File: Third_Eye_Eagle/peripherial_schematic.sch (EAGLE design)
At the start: 1 part

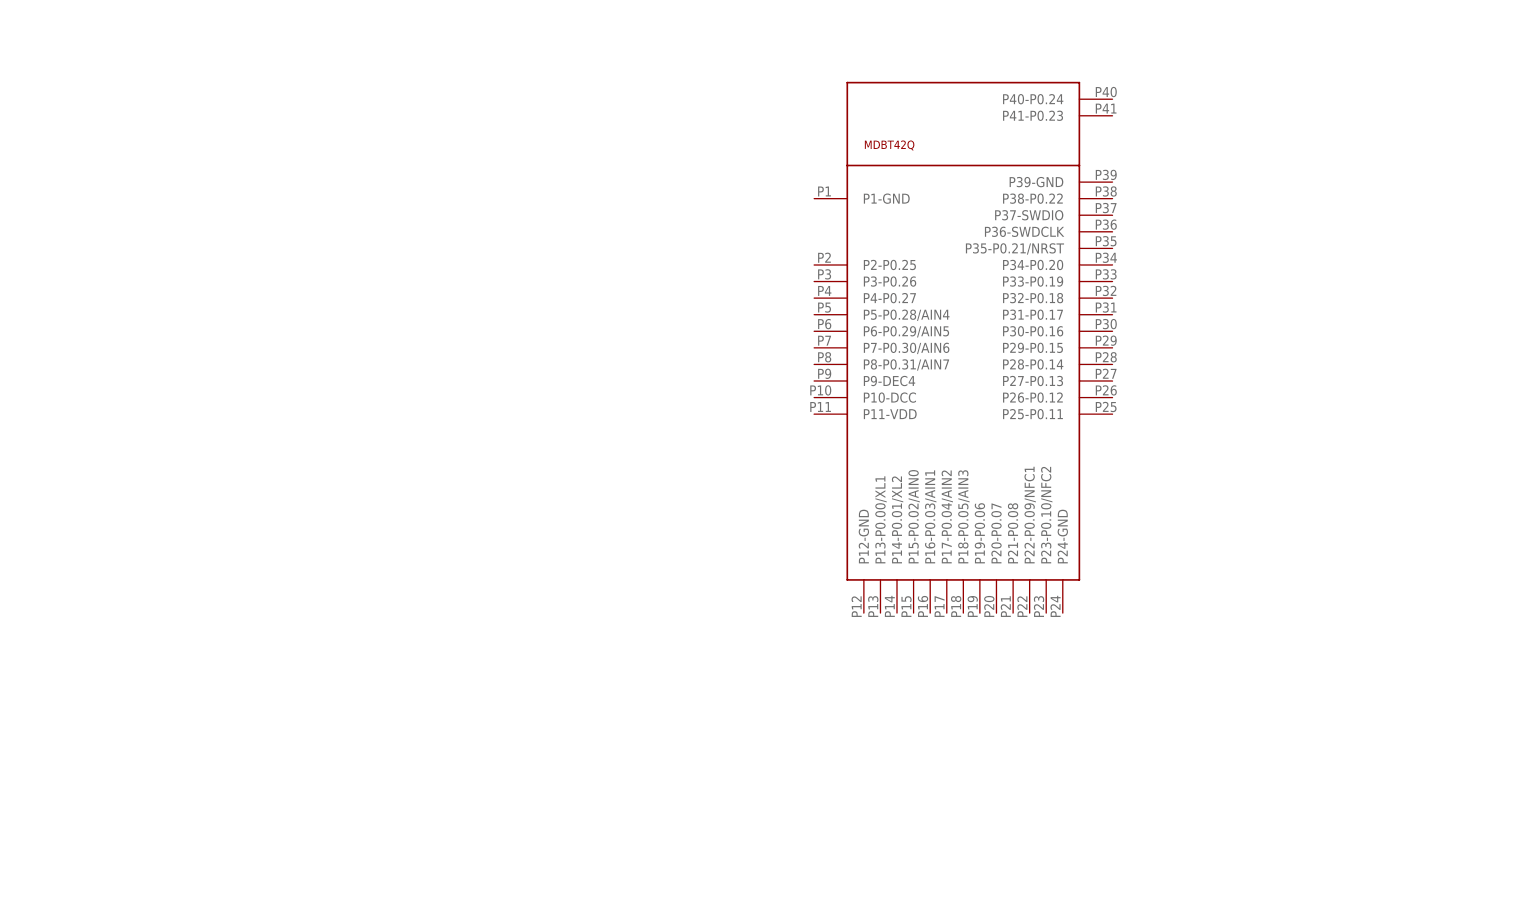
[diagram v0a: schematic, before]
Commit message: Updated Eagle LIbrary and git ignore the eagle temp files
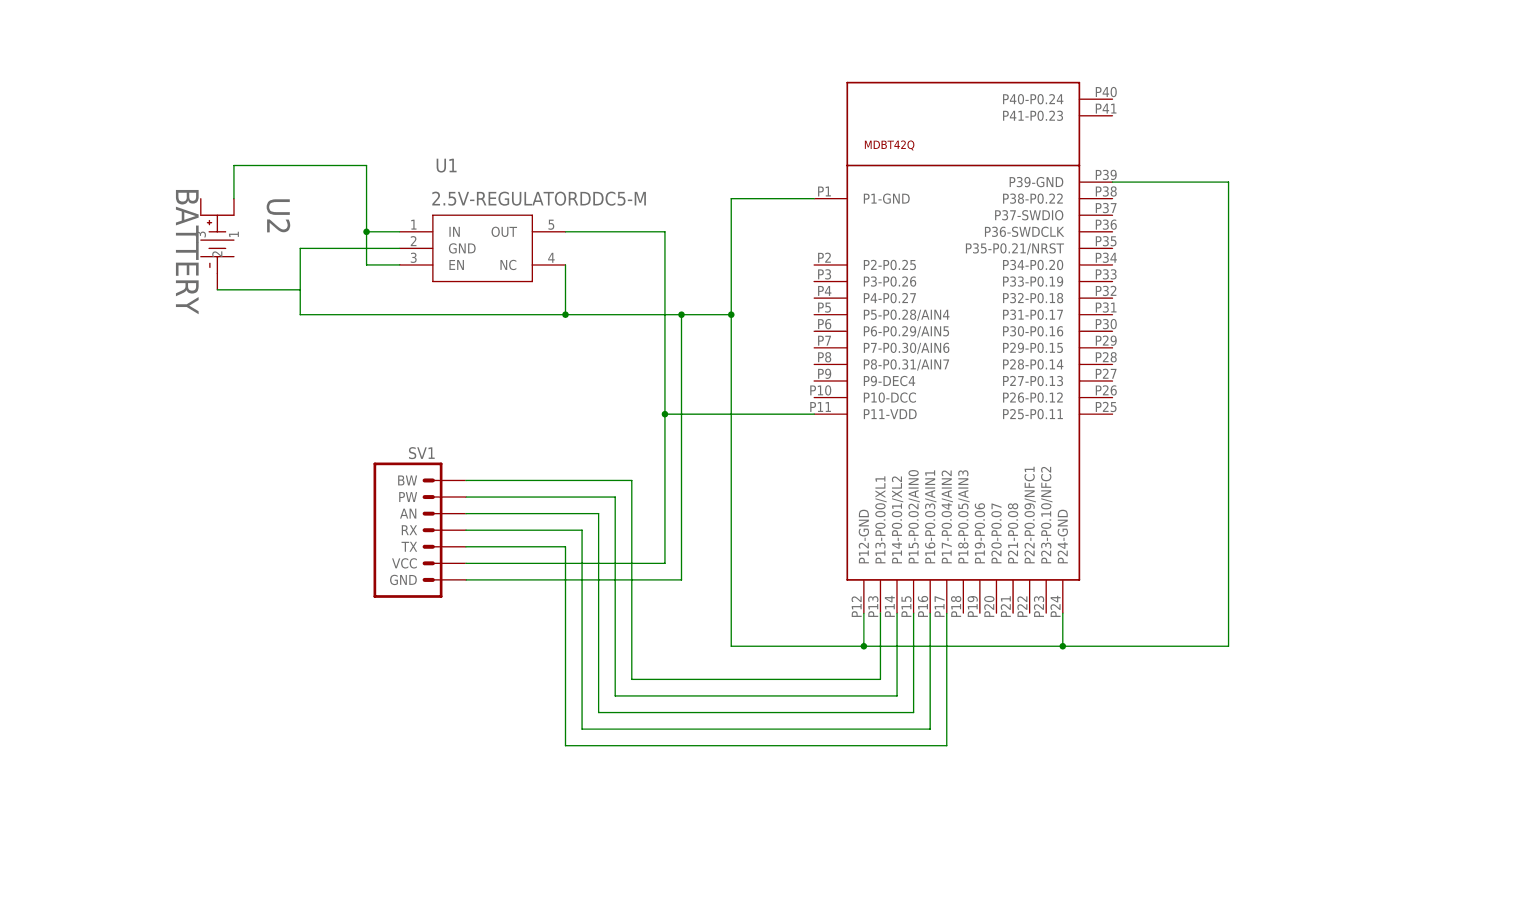
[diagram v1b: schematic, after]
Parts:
- added SV1: (no value), third_eye:SENSORHEADER
- added U1: 2.5V-REGULATORDDC5-M, third_eye:2.5V-REGULATORDDC5-M
- added U2: BATTERY, third_eye:BATTERY
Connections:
- new net N$1: U1.EN, U1.IN, U2.1
- new net N$2: SV1.GND, U$1.P1-GND, U$1.P12-GND, U$1.P24-GND, U$1.P39-GND, U1.GND, U1.NC, U2.2
- new net N$3: SV1.AN, U$1.P15-P0.02/AIN0
- new net N$4: SV1.VCC, U$1.P11-VDD, U1.OUT
- new net N$5: SV1.PW, U$1.P14-P0.01/XL2
- new net N$7: SV1.RX, U$1.P16-P0.03/AIN1
- new net N$8: SV1.TX, U$1.P17-P0.04/AIN2
- new net N$9: SV1.BW, U$1.P13-P0.00/XL1
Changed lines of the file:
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@@
 <setting verticaltext="up"/>
 </settings>
-<grid distance="0.1" unitdist="inch" unit="inch" style="lines" multiple="1" display="no" altdistance="0.01" altunitdist="inch" altunit="inch"/>
+<grid distance="0.1" unitdist="inch" unit="inch" style="dots" multiple="1" display="yes" altdistance="0.01" altunitdist="inch" altunit="inch"/>
 <layers>
 <layer number="1" name="Top" color="4" fill="1" visible="no" active="no"/>
@@
 <parts>
 <part name="U$1" library="third_eye" deviceset="MDBT42Q" device=""/>
+<part name="SV1" library="third_eye" deviceset="SENSORHEADER" device="" package3d_urn="urn:adsk.eagle:package:8341/1"/>
+<part name="U2" library="third_eye" deviceset="BATTERY" device=""/>
+<part name="U1" library="third_eye" deviceset="2.5V-REGULATOR" device="DDC5-M"/>
 </parts>
 <sheets>
@@
 <instances>
 <instance part="U$1" gate="G$1" x="58.42" y="53.34" smashed="yes"/>
+<instance part="SV1" gate="1" x="-38.1" y="20.32" smashed="yes">
+<attribute name="VALUE" x="-39.37" y="7.62" size="1.778" layer="96"/>
+<attribute name="NAME" x="-39.37" y="31.242" size="1.778" layer="95"/>
+</instance>
+<instance part="U2" gate="BAT" x="-66.04" y="71.12" smashed="yes" rot="R270">
+<attribute name="NAME" x="-60.96" y="71.3994" size="3.4798" layer="95" ratio="10" rot="SR270"/>
+<attribute name="VALUE" x="-74.93" y="72.8726" size="3.4798" layer="96" ratio="10" rot="SR270"/>
+</instance>
+<instance part="U1" gate="A" x="-43.18" y="66.04" smashed="yes">
+<attribute name="NAME" x="-35.2044" y="75.1586" size="2.0828" layer="95" ratio="6" rot="SR0"/>
+<attribute name="VALUE" x="-35.8394" y="70.0786" size="2.0828" layer="96" ratio="6" rot="SR0"/>
+</instance>
 </instances>
 <busses>
 </busses>
 <nets>
+<net name="N$1" class="0">
+<segment>
+<pinref part="U1" gate="A" pin="IN"/>
+<wire x1="-40.64" y1="66.04" x2="-45.72" y2="66.04" width="0.1524" layer="91"/>
+<wire x1="-45.72" y1="66.04" x2="-45.72" y2="76.2" width="0.1524" layer="91"/>
+<wire x1="-45.72" y1="76.2" x2="-66.04" y2="76.2" width="0.1524" layer="91"/>
+<pinref part="U2" gate="BAT" pin="1"/>
+<wire x1="-66.04" y1="76.2" x2="-66.04" y2="71.12" width="0.1524" layer="91"/>
+<pinref part="U1" gate="A" pin="EN"/>
+<wire x1="-40.64" y1="60.96" x2="-45.72" y2="60.96" width="0.1524" layer="91"/>
+<wire x1="-45.72" y1="60.96" x2="-45.72" y2="66.04" width="0.1524" layer="91"/>
+<junction x="-45.72" y="66.04"/>
+</segment>
+</net>
+<net name="N$2" class="0">
+<segment>
+<pinref part="U2" gate="BAT" pin="2"/>
+<wire x1="-68.58" y1="57.15" x2="-55.88" y2="57.15" width="0.1524" layer="91"/>
+<pinref part="U1" gate="A" pin="GND"/>
+<wire x1="-55.88" y1="57.15" x2="-55.88" y2="63.5" width="0.1524" layer="91"/>
+<wire x1="-55.88" y1="63.5" x2="-40.64" y2="63.5" width="0.1524" layer="91"/>
+<pinref part="U1" gate="A" pin="NC"/>
+<wire x1="-15.24" y1="60.96" x2="-15.24" y2="53.34" width="0.1524" layer="91"/>
+<wire x1="-15.24" y1="53.34" x2="-55.88" y2="53.34" width="0.1524" layer="91"/>
+<wire x1="-55.88" y1="53.34" x2="-55.88" y2="57.15" width="0.1524" layer="91"/>
+<wire x1="-15.24" y1="53.34" x2="2.54" y2="53.34" width="0.1524" layer="91"/>
+<wire x1="2.54" y1="53.34" x2="10.16" y2="53.34" width="0.1524" layer="91"/>
+<wire x1="10.16" y1="53.34" x2="10.16" y2="71.12" width="0.1524" layer="91"/>
+<junction x="-15.24" y="53.34"/>
+<pinref part="U$1" gate="G$1" pin="P1-GND"/>
+<wire x1="10.16" y1="71.12" x2="22.86" y2="71.12" width="0.1524" layer="91"/>
+<pinref part="U$1" gate="G$1" pin="P12-GND"/>
+<wire x1="30.48" y1="7.62" x2="30.48" y2="2.54" width="0.1524" layer="91"/>
+<wire x1="30.48" y1="2.54" x2="10.16" y2="2.54" width="0.1524" layer="91"/>
+<wire x1="10.16" y1="2.54" x2="10.16" y2="53.34" width="0.1524" layer="91"/>
+<junction x="10.16" y="53.34"/>
+<pinref part="SV1" gate="1" pin="GND"/>
+<wire x1="-30.48" y1="12.7" x2="2.54" y2="12.7" width="0.1524" layer="91"/>
+<wire x1="2.54" y1="12.7" x2="2.54" y2="53.34" width="0.1524" layer="91"/>
+<junction x="2.54" y="53.34"/>
+<wire x1="30.48" y1="2.54" x2="60.96" y2="2.54" width="0.1524" layer="91"/>
+<junction x="30.48" y="2.54"/>
+<pinref part="U$1" gate="G$1" pin="P24-GND"/>
+<wire x1="60.96" y1="2.54" x2="60.96" y2="7.62" width="0.1524" layer="91"/>
+<pinref part="U$1" gate="G$1" pin="P39-GND"/>
+<wire x1="68.58" y1="73.66" x2="86.36" y2="73.66" width="0.1524" layer="91"/>
+<wire x1="86.36" y1="73.66" x2="86.36" y2="2.54" width="0.1524" layer="91"/>
+<wire x1="86.36" y1="2.54" x2="60.96" y2="2.54" width="0.1524" layer="91"/>
+<junction x="60.96" y="2.54"/>
+</segment>
+</net>
+<net name="N$4" class="0">
+<segment>
+<pinref part="U1" gate="A" pin="OUT"/>
+<wire x1="-15.24" y1="66.04" x2="0" y2="66.04" width="0.1524" layer="91"/>
+<wire x1="0" y1="66.04" x2="0" y2="38.1" width="0.1524" layer="91"/>
+<pinref part="U$1" gate="G$1" pin="P11-VDD"/>
+<wire x1="0" y1="38.1" x2="22.86" y2="38.1" width="0.1524" layer="91"/>
+<pinref part="SV1" gate="1" pin="VCC"/>
+<wire x1="-30.48" y1="15.24" x2="0" y2="15.24" width="0.1524" layer="91"/>
+<wire x1="0" y1="15.24" x2="0" y2="38.1" width="0.1524" layer="91"/>
+<junction x="0" y="38.1"/>
+</segment>
+</net>
+<net name="N$3" class="0">
+<segment>
+<pinref part="U$1" gate="G$1" pin="P15-P0.02/AIN0"/>
+<wire x1="38.1" y1="7.62" x2="38.1" y2="-7.62" width="0.1524" layer="91"/>
+<wire x1="38.1" y1="-7.62" x2="-10.16" y2="-7.62" width="0.1524" layer="91"/>
+<wire x1="-10.16" y1="-7.62" x2="-10.16" y2="22.86" width="0.1524" layer="91"/>
+<pinref part="SV1" gate="1" pin="AN"/>
+<wire x1="-10.16" y1="22.86" x2="-30.48" y2="22.86" width="0.1524" layer="91"/>
+</segment>
+</net>
+<net name="N$5" class="0">
+<segment>
+<pinref part="U$1" gate="G$1" pin="P14-P0.01/XL2"/>
+<wire x1="35.56" y1="7.62" x2="35.56" y2="-5.08" width="0.1524" layer="91"/>
+<wire x1="35.56" y1="-5.08" x2="-7.62" y2="-5.08" width="0.1524" layer="91"/>
+<wire x1="-7.62" y1="-5.08" x2="-7.62" y2="25.4" width="0.1524" layer="91"/>
+<pinref part="SV1" gate="1" pin="PW"/>
+<wire x1="-7.62" y1="25.4" x2="-30.48" y2="25.4" width="0.1524" layer="91"/>
+</segment>
+</net>
+<net name="N$7" class="0">
+<segment>
+<pinref part="U$1" gate="G$1" pin="P16-P0.03/AIN1"/>
+<wire x1="40.64" y1="7.62" x2="40.64" y2="-10.16" width="0.1524" layer="91"/>
+<wire x1="40.64" y1="-10.16" x2="-12.7" y2="-10.16" width="0.1524" layer="91"/>
+<wire x1="-12.7" y1="-10.16" x2="-12.7" y2="20.32" width="0.1524" layer="91"/>
+<pinref part="SV1" gate="1" pin="RX"/>
+<wire x1="-12.7" y1="20.32" x2="-30.48" y2="20.32" width="0.1524" layer="91"/>
+</segment>
+</net>
+<net name="N$8" class="0">
+<segment>
+<pinref part="SV1" gate="1" pin="TX"/>
+<wire x1="-30.48" y1="17.78" x2="-15.24" y2="17.78" width="0.1524" layer="91"/>
+<wire x1="-15.24" y1="17.78" x2="-15.24" y2="-12.7" width="0.1524" layer="91"/>
+<wire x1="-15.24" y1="-12.7" x2="43.18" y2="-12.7" width="0.1524" layer="91"/>
+<pinref part="U$1" gate="G$1" pin="P17-P0.04/AIN2"/>
+<wire x1="43.18" y1="-12.7" x2="43.18" y2="7.62" width="0.1524" layer="91"/>
+</segment>
+</net>
+<net name="N$9" class="0">
+<segment>
+<pinref part="U$1" gate="G$1" pin="P13-P0.00/XL1"/>
+<wire x1="33.02" y1="7.62" x2="33.02" y2="-2.54" width="0.1524" layer="91"/>
+<wire x1="33.02" y1="-2.54" x2="-5.08" y2="-2.54" width="0.1524" layer="91"/>
+<wire x1="-5.08" y1="-2.54" x2="-5.08" y2="27.94" width="0.1524" layer="91"/>
+<pinref part="SV1" gate="1" pin="BW"/>
+<wire x1="-5.08" y1="27.94" x2="-30.48" y2="27.94" width="0.1524" layer="91"/>
+</segment>
+</net>
 </nets>
 </sheet>
@@
 </schematic>
 </drawing>
+<compatibility>
+<note version="8.3" severity="warning">
+Since Version 8.3, EAGLE supports URNs for individual library
+assets (packages, symbols, and devices). The URNs of those assets
+will not be understood (or retained) with this version.
+</note>
+<note version="8.3" severity="warning">
+Since Version 8.3, EAGLE supports the association of 3D packages
+with devices in libraries, schematics, and board files. Those 3D
+packages will not be understood (or retained) with this version.
+</note>
+</compatibility>
 </eagle>

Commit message: Eagle library updates and schematic changes
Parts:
- removed SV1: (no value), third_eye:SENSORHEADER
- removed U2: BATTERY, third_eye:BATTERY
- added BATT: BATTERY, third_eye:BATTERY
- added DEBUG: (no value), third_eye:DEBUGGER
- added SENSOR: (no value), third_eye:SENSORHEADER
- added U$2, U$3, U$4, U$5, U$6, U$7: CAP, third_eye:CAP
- renumbered U$1 to MICRO, U1 to 2.5V
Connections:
- new net N$11: DEBUG.SWCLK, MICRO.P36-SWDCLK
- new net N$12: DEBUG.SWDIO, MICRO.P37-SWDIO
- new net N$13: DEBUG.NRST, MICRO.P35-P0.21/NRST
- net N$1: now also BATT.1, U$5.1; no longer U2.1
- net N$2: now also BATT.2, DEBUG.GND, SENSOR.GND, U$2.2, U$3.2, U$4.1, U$5.2, U$6.2; no longer SV1.GND, U2.2
- net N$3: now also SENSOR.AN; no longer SV1.AN
- net N$4: now also DEBUG.VREF, SENSOR.VCC, U$2.1, U$3.1, U$4.2, U$6.1; no longer SV1.VCC
- net N$5: now also SENSOR.PW; no longer SV1.PW
- net N$7: now also SENSOR.RX; no longer SV1.RX
- net N$8: now also SENSOR.TX; no longer SV1.TX
- net N$9: now also SENSOR.BW; no longer SV1.BW

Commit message: My new branch
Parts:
- added U$1: RESISTOR, third_eye:RESISTOR
- added U$8: BUTTON, third_eye:BUTTON
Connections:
- removed net N$13: DEBUG.NRST, MICRO.P35-P0.21/NRST
- removed net N$8: MICRO.P17-P0.04/AIN2, SENSOR.TX
- net N$2: now also U$7.2, U$8.2
- net N$4: now also U$1.2
- net N$7: now also DEBUG.NRST, MICRO.P35-P0.21/NRST, U$1.1, U$7.1, U$8.1; no longer MICRO.P16-P0.03/AIN1, SENSOR.RX
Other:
- moved on the sheet: U$7

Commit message: Updating eagle library again to merge with alex
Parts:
- added D1: WHITE, third_eye:LED_12061206
- added SV1: (no value), third_eye:GPIO
- added U$9: RESISTOR, third_eye:RESISTOR
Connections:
- new net N$10: MICRO.P16-P0.03/AIN1, SV1.GPIO1
- new net N$13: MICRO.P19-P0.06, SV1.GPIO2
- new net N$14: MICRO.P20-P0.07, SV1.GPIO3
- new net N$6: D1.A, MICRO.P25-P0.11
- new net N$8: D1.C, U$9.2
- net N$2: now also U$9.1
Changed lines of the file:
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@@
 <layer number="112" name="tSilk" color="7" fill="1" visible="no" active="yes"/>
 <layer number="113" name="IDFDebug" color="4" fill="1" visible="no" active="yes"/>
+<layer number="114" name="Badge_Outline" color="7" fill="1" visible="yes" active="yes"/>
+<layer number="115" name="ReferenceISLANDS" color="7" fill="1" visible="yes" active="yes"/>
 <layer number="116" name="Patch_BOT" color="9" fill="4" visible="no" active="yes"/>
 <layer number="118" name="Rect_Pads" color="7" fill="1" visible="no" active="yes"/>
@@
 <layer number="230" name="230bmp" color="7" fill="1" visible="no" active="yes"/>
 <layer number="231" name="231bmp" color="7" fill="1" visible="no" active="yes"/>
+<layer number="232" name="Eagle3D_PG2" color="7" fill="1" visible="yes" active="yes"/>
+<layer number="233" name="Eagle3D_PG3" color="7" fill="1" visible="yes" active="yes"/>
 <layer number="248" name="Housing" color="7" fill="1" visible="no" active="yes"/>
 <layer number="249" name="Edge" color="7" fill="1" visible="no" active="yes"/>
@@
 <part name="U$1" library="third_eye" deviceset="RESISTOR" device=""/>
 <part name="U$8" library="third_eye" deviceset="BUTTON" device=""/>
+<part name="D1" library="third_eye" deviceset="LED_1206" device="1206" package3d_urn="urn:adsk.eagle:package:39352/1" value="WHITE"/>
+<part name="U$9" library="third_eye" deviceset="RESISTOR" device=""/>
+<part name="SV1" library="third_eye" deviceset="GPIO" device="" package3d_urn="urn:adsk.eagle:package:8339/1"/>
 </parts>
 <sheets>
@@
 <attribute name="NAME" x="100.584" y="38.1" size="1.778" layer="95" font="vector" rot="R270" align="bottom-center"/>
 <attribute name="VALUE" x="98.552" y="38.1" size="1.778" layer="96" font="vector" rot="R270" align="top-center"/>
+</instance>
+<instance part="D1" gate="G$1" x="93.98" y="7.62" smashed="yes">
+<attribute name="NAME" x="90.551" y="3.048" size="1.778" layer="95" font="vector" rot="R90"/>
+<attribute name="VALUE" x="95.885" y="3.048" size="1.778" layer="96" font="vector" rot="R90" align="top-left"/>
+</instance>
+<instance part="U$9" gate="G$1" x="93.98" y="-5.08" smashed="yes" rot="R90">
+<attribute name="NAME" x="92.4814" y="-8.89" size="1.778" layer="95" rot="R90"/>
+<attribute name="VALUE" x="97.282" y="-8.89" size="1.778" layer="96" rot="R90"/>
+</instance>
+<instance part="SV1" gate="G$1" x="25.4" y="-30.48" smashed="yes">
+<attribute name="VALUE" x="24.13" y="-38.1" size="1.778" layer="96"/>
+<attribute name="NAME" x="24.13" y="-24.638" size="1.778" layer="95"/>
 </instance>
 </instances>
@@
 <wire x1="81.28" y1="73.66" x2="81.28" y2="27.94" width="0.1524" layer="91"/>
 <wire x1="81.28" y1="27.94" x2="81.28" y2="2.54" width="0.1524" layer="91"/>
-<wire x1="81.28" y1="2.54" x2="60.96" y2="2.54" width="0.1524" layer="91"/>
+<wire x1="81.28" y1="2.54" x2="73.66" y2="2.54" width="0.1524" layer="91"/>
 <junction x="60.96" y="2.54"/>
 <pinref part="U$2" gate="G$1" pin="2"/>
+<wire x1="73.66" y1="2.54" x2="60.96" y2="2.54" width="0.1524" layer="91"/>
 <wire x1="20.32" y1="5.08" x2="20.32" y2="2.54" width="0.1524" layer="91"/>
 <junction x="20.32" y="2.54"/>
@@
 <wire x1="99.06" y1="27.94" x2="86.36" y2="27.94" width="0.1524" layer="91"/>
 <junction x="86.36" y="27.94"/>
+<pinref part="U$9" gate="G$1" pin="1"/>
+<wire x1="93.98" y1="-10.16" x2="73.66" y2="-10.16" width="0.1524" layer="91"/>
+<wire x1="73.66" y1="-10.16" x2="73.66" y2="2.54" width="0.1524" layer="91"/>
+<junction x="73.66" y="2.54"/>
 </segment>
 </net>
@@
 <wire x1="33.02" y1="-2.54" x2="-5.08" y2="-2.54" width="0.1524" layer="91"/>
 <wire x1="-5.08" y1="-2.54" x2="-5.08" y2="27.94" width="0.1524" layer="91"/>
+<wire x1="-5.08" y1="27.94" x2="-55.88" y2="27.94" width="0.1524" layer="91"/>
 <pinref part="SENSOR" gate="1" pin="BW"/>
-<wire x1="-5.08" y1="27.94" x2="-55.88" y2="27.94" width="0.1524" layer="91"/>
 </segment>
 </net>
@@
 </segment>
 </net>
+<net name="N$6" class="0">
+<segment>
+<pinref part="MICRO" gate="G$1" pin="P25-P0.11"/>
+<wire x1="68.58" y1="38.1" x2="76.2" y2="38.1" width="0.1524" layer="91"/>
+<wire x1="76.2" y1="38.1" x2="76.2" y2="15.24" width="0.1524" layer="91"/>
+<wire x1="76.2" y1="15.24" x2="93.98" y2="15.24" width="0.1524" layer="91"/>
+<pinref part="D1" gate="G$1" pin="A"/>
+<wire x1="93.98" y1="15.24" x2="93.98" y2="10.16" width="0.1524" layer="91"/>
+</segment>
+</net>
+<net name="N$8" class="0">
+<segment>
+<pinref part="D1" gate="G$1" pin="C"/>
+<pinref part="U$9" gate="G$1" pin="2"/>
+<wire x1="93.98" y1="2.54" x2="93.98" y2="0" width="0.1524" layer="91"/>
+</segment>
+</net>
+<net name="N$10" class="0">
+<segment>
+<pinref part="MICRO" gate="G$1" pin="P16-P0.03/AIN1"/>
+<wire x1="40.64" y1="7.62" x2="40.64" y2="-27.94" width="0.1524" layer="91"/>
+<pinref part="SV1" gate="G$1" pin="GPIO1"/>
+<wire x1="40.64" y1="-27.94" x2="33.02" y2="-27.94" width="0.1524" layer="91"/>
+</segment>
+</net>
+<net name="N$13" class="0">
+<segment>
+<pinref part="MICRO" gate="G$1" pin="P19-P0.06"/>
+<pinref part="SV1" gate="G$1" pin="GPIO2"/>
+<wire x1="48.26" y1="7.62" x2="48.26" y2="-30.48" width="0.1524" layer="91"/>
+<wire x1="48.26" y1="-30.48" x2="33.02" y2="-30.48" width="0.1524" layer="91"/>
+</segment>
+</net>
+<net name="N$14" class="0">
+<segment>
+<pinref part="MICRO" gate="G$1" pin="P20-P0.07"/>
+<pinref part="SV1" gate="G$1" pin="GPIO3"/>
+<wire x1="50.8" y1="7.62" x2="50.8" y2="-33.02" width="0.1524" layer="91"/>
+<wire x1="50.8" y1="-33.02" x2="33.02" y2="-33.02" width="0.1524" layer="91"/>
+</segment>
+</net>
